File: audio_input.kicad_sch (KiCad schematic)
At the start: 4 parts

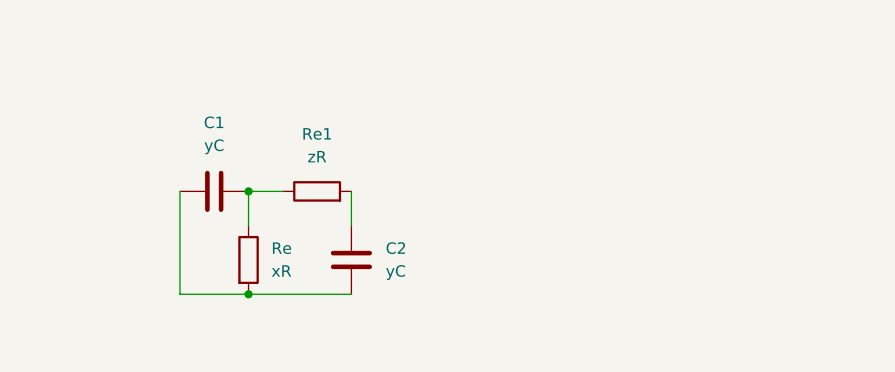
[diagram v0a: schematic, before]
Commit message: Rev 1
needs sensors, things like pull-up resistors and protection diodes, electrical rules check. also check SCL and SDA busses, variable resistors
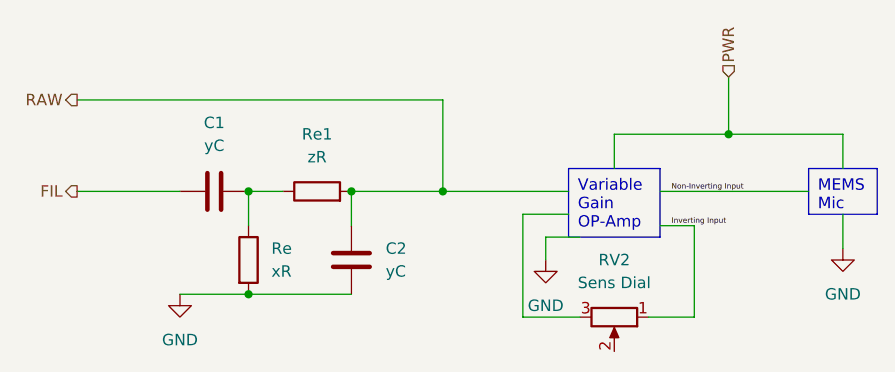
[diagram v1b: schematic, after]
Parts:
- added RV2: Sens Dial, Potentiometer_SMD:Potentiometer_ACP_CA6-VSMD_Vertical, symbol Device:R_Potentiometer
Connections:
- net GND: now reaches C2.1, Re.2
- net GND: no longer C1.1
- net RAW: now reaches C2.2, Re1.2
- new net FIL: C1.1
- new net Inverting Input: RV2.1
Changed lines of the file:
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@@
   (junction (at 148.59 92.71) (diameter 0) (color 0 0 0 0)
   )
+  (junction (at 201.93 86.36) (diameter 0) (color 0 0 0 0)
+  )
+  (junction (at 160.02 92.71) (diameter 0) (color 0 0 0 0)
+  )
+  (junction (at 170.18 92.71) (diameter 0) (color 0 0 0 0)
+  )
   (junction (at 148.59 104.14) (diameter 0) (color 0 0 0 0)
   )
+  (wire (pts (xy 181.61 97.79) (xy 181.61 100.33))
+    (stroke (width 0) (type default))
+  )
+  (wire (pts (xy 184.15 95.25) (xy 179.07 95.25))
+    (stroke (width 0) (type default))
+  )
+  (wire (pts (xy 185.42 97.79) (xy 181.61 97.79))
+    (stroke (width 0) (type default))
+  )
+  (wire (pts (xy 179.07 106.68) (xy 185.42 106.68))
+    (stroke (width 0) (type default))
+  )
+  (wire (pts (xy 198.12 106.68) (xy 198.12 96.52))
+    (stroke (width 0) (type default))
+  )
+  (wire (pts (xy 214.63 95.25) (xy 214.63 99.06))
+    (stroke (width 0) (type default))
+  )
+  (wire (pts (xy 194.31 92.71) (xy 210.82 92.71))
+    (stroke (width 0) (type default))
+  )
   (wire (pts (xy 140.97 104.14) (xy 148.59 104.14))
     (stroke (width 0) (type default))
@@
     (stroke (width 0) (type default))
   )
-  (wire (pts (xy 140.97 92.71) (xy 140.97 104.14))
+  (wire (pts (xy 179.07 95.25) (xy 179.07 106.68))
+    (stroke (width 0) (type default))
+  )
+  (wire (pts (xy 194.31 96.52) (xy 198.12 96.52))
     (stroke (width 0) (type default))
   )
@@
     (stroke (width 0) (type default))
   )
+  (wire (pts (xy 129.54 82.55) (xy 170.18 82.55))
+    (stroke (width 0) (type default))
+  )
+  (wire (pts (xy 201.93 80.01) (xy 201.93 86.36))
+    (stroke (width 0) (type default))
+  )
+  (wire (pts (xy 193.04 106.68) (xy 198.12 106.68))
+    (stroke (width 0) (type default))
+  )
+  (wire (pts (xy 160.02 92.71) (xy 170.18 92.71))
+    (stroke (width 0) (type default))
+  )
+  (wire (pts (xy 201.93 86.36) (xy 189.23 86.36))
+    (stroke (width 0) (type default))
+  )
   (wire (pts (xy 148.59 104.14) (xy 160.02 104.14))
     (stroke (width 0) (type default))
   )
+  (wire (pts (xy 184.15 92.71) (xy 170.18 92.71))
+    (stroke (width 0) (type default))
+  )
+  (wire (pts (xy 189.23 86.36) (xy 189.23 90.17))
+    (stroke (width 0) (type default))
+  )
+  (wire (pts (xy 170.18 82.55) (xy 170.18 92.71))
+    (stroke (width 0) (type default))
+  )
+  (wire (pts (xy 129.54 92.71) (xy 140.97 92.71))
+    (stroke (width 0) (type default))
+  )
   (wire (pts (xy 160.02 92.71) (xy 160.02 96.52))
     (stroke (width 0) (type default))
+  )
+  (wire (pts (xy 214.63 86.36) (xy 201.93 86.36))
+    (stroke (width 0) (type default))
+  )
+  (wire (pts (xy 214.63 90.17) (xy 214.63 86.36))
+    (stroke (width 0) (type default))
+  )
+  (text_box "Variable Gain OP-Amp"
+    (at 184.15 90.17 0) (size 10.16 7.62)
+    (stroke (width 0) (type default))
+    (fill (type none))
+    (effects (font (size 1.27 1.27)) (justify left top))
+  )
+  (text_box "MEMS Mic"
+    (at 210.82 90.17 0) (size 7.62 5.08)
+    (stroke (width 0) (type default))
+    (fill (type none))
+    (effects (font (size 1.27 1.27)) (justify left top))
+  )
+  (label "Non-Inverting Input" (at 195.58 92.71 0) (fields_autoplaced)
+    (effects (font (size 0.6 0.6)) (justify left bottom))
+  )
+  (label "Inverting Input" (at 195.58 96.52 0) (fields_autoplaced)
+    (effects (font (size 0.6 0.6)) (justify left bottom))
+  )
+  (hierarchical_label "FIL" (shape output) (at 129.54 92.71 180) (fields_autoplaced)
+    (effects (font (size 1.27 1.27)) (justify right))
+  )
+  (hierarchical_label "PWR" (shape input) (at 201.93 80.01 90) (fields_autoplaced)
+    (effects (font (size 1.27 1.27)) (justify left))
+  )
+  (hierarchical_label "RAW" (shape output) (at 129.54 82.55 180) (fields_autoplaced)
+    (effects (font (size 1.27 1.27)) (justify right))
   )
   (symbol (lib_id "Device:C") (at 160.02 100.33 180) (unit 1)
@@
         )
       )
+    )
+  )
+  (symbol (lib_id "power:GND") (at 181.61 100.33 0) (unit 1)
+    (in_bom yes) (on_board yes) (dnp no) (fields_autoplaced)
+    (property "Reference" "#PWR03" (at 181.61 106.68 0)
+      (effects (font (size 1.27 1.27)) hide)
+    )
+    (property "Value" "GND" (at 181.61 105.41 0)
+      (effects (font (size 1.27 1.27)))
+    )
+    (property "Footprint" "" (at 181.61 100.33 0)
+      (effects (font (size 1.27 1.27)) hide)
+    )
+    (property "Datasheet" "" (at 181.61 100.33 0)
+      (effects (font (size 1.27 1.27)) hide)
+    )
+    (pin "1")
+    (instances
+      (project "VibeLight"
+        (path "/704dec10-a4c2-4298-be85-193d9407f59f/964563b4-99e1-4b3d-857d-35f5fde5aa09"
+          (reference "#PWR03") (unit 1)
+        )
+      )
+    )
+  )
+  (symbol (lib_id "power:GND") (at 214.63 99.06 0) (unit 1)
+    (in_bom yes) (on_board yes) (dnp no) (fields_autoplaced)
+    (property "Reference" "#PWR02" (at 214.63 105.41 0)
+      (effects (font (size 1.27 1.27)) hide)
+    )
+    (property "Value" "GND" (at 214.63 104.14 0)
+      (effects (font (size 1.27 1.27)))
+    )
+    (property "Footprint" "" (at 214.63 99.06 0)
+      (effects (font (size 1.27 1.27)) hide)
+    )
+    (property "Datasheet" "" (at 214.63 99.06 0)
+      (effects (font (size 1.27 1.27)) hide)
+    )
+    (pin "1")
+    (instances
+      (project "VibeLight"
+        (path "/704dec10-a4c2-4298-be85-193d9407f59f/964563b4-99e1-4b3d-857d-35f5fde5aa09"
+          (reference "#PWR02") (unit 1)
+        )
+      )
+    )
+  )
+  (symbol (lib_id "Device:R_Potentiometer") (at 189.23 106.68 270) (unit 1)
+    (in_bom yes) (on_board yes) (dnp no) (fields_autoplaced)
+    (property "Reference" "RV2" (at 189.23 100.33 90)
+      (effects (font (size 1.27 1.27)))
+    )
+    (property "Value" "Sens Dial" (at 189.23 102.87 90)
+      (effects (font (size 1.27 1.27)))
+    )
+    (property "Footprint" "Potentiometer_SMD:Potentiometer_ACP_CA6-VSMD_Vertical" (at 189.23 106.68 0)
+      (effects (font (size 1.27 1.27)) hide)
+    )
+    (property "Datasheet" "~" (at 189.23 106.68 0)
+      (effects (font (size 1.27 1.27)) hide)
+    )
+    (pin "1")
+    (pin "2")
+    (pin "3")
+    (instances
+      (project "VibeLight"
+        (path "/704dec10-a4c2-4298-be85-193d9407f59f"
+          (reference "RV2") (unit 1)
+        )
+        (path "/704dec10-a4c2-4298-be85-193d9407f59f/964563b4-99e1-4b3d-857d-35f5fde5aa09"
+          (reference "RV1") (unit 1)
+        )
+      )
+    )
+  )
+  (symbol (lib_id "power:GND") (at 140.97 104.14 0) (unit 1)
+    (in_bom yes) (on_board yes) (dnp no) (fields_autoplaced)
+    (property "Reference" "#PWR01" (at 140.97 110.49 0)
+      (effects (font (size 1.27 1.27)) hide)
+    )
+    (property "Value" "GND" (at 140.97 109.22 0)
+      (effects (font (size 1.27 1.27)))
+    )
+    (property "Footprint" "" (at 140.97 104.14 0)
+      (effects (font (size 1.27 1.27)) hide)
+    )
+    (property "Datasheet" "" (at 140.97 104.14 0)
+      (effects (font (size 1.27 1.27)) hide)
+    )
+    (pin "1")
+    (instances
+      (project "VibeLight"
+        (path "/704dec10-a4c2-4298-be85-193d9407f59f/964563b4-99e1-4b3d-857d-35f5fde5aa09"
+          (reference "#PWR01") (unit 1)
+        )
+      )

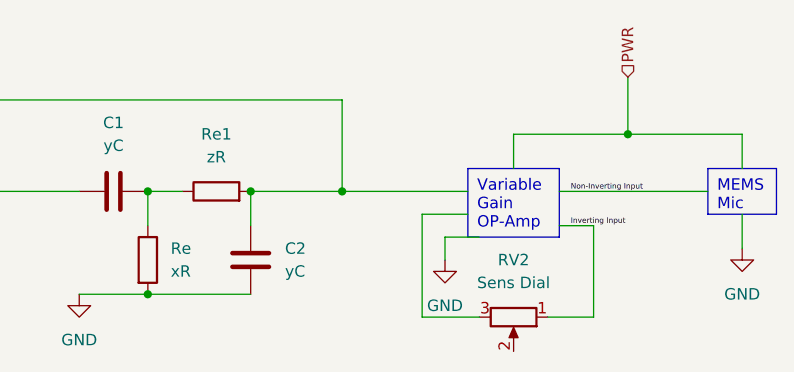
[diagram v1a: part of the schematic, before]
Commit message: added debug LED after Op-Amp
want battery status LED?
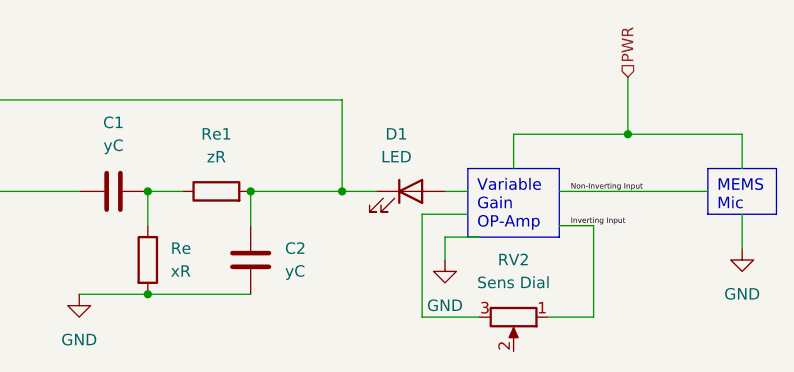
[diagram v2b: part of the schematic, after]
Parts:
- added D1: LED, symbol Device:LED
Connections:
- net RAW: now also D1.1 (K)
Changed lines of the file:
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@@
+    (stroke (width 0) (type default))
+  )
+  (wire (pts (xy 170.18 92.71) (xy 173.99 92.71))
     (stroke (width 0) (type default))
   )
@@
     (stroke (width 0) (type default))
   )
-  (wire (pts (xy 184.15 92.71) (xy 170.18 92.71))
+  (wire (pts (xy 181.61 92.71) (xy 184.15 92.71))
     (stroke (width 0) (type default))
   )
@@
         )
       )
+    )
+  )
+  (symbol (lib_id "Device:LED") (at 177.8 92.71 0) (unit 1)
+    (in_bom yes) (on_board yes) (dnp no) (fields_autoplaced)
+    (property "Reference" "D1" (at 176.2125 86.36 0)
+      (effects (font (size 1.27 1.27)))
+    )
+    (property "Value" "LED" (at 176.2125 88.9 0)
+      (effects (font (size 1.27 1.27)))
+    )
+    (property "Footprint" "" (at 177.8 92.71 0)
+      (effects (font (size 1.27 1.27)) hide)
+    )
+    (property "Datasheet" "~" (at 177.8 92.71 0)
+      (effects (font (size 1.27 1.27)) hide)
+    )
+    (pin "1")
+    (pin "2")
+    (instances
+      (project "VibeLight"
+        (path "/704dec10-a4c2-4298-be85-193d9407f59f/964563b4-99e1-4b3d-857d-35f5fde5aa09"
+          (reference "D1") (unit 1)
+        )
+      )

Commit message: misc changes during call
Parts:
- added Re: xR, Resistor_SMD:R_0603_1608Metric_Pad0.98x0.95mm_HandSolder, symbol Device:R
- D1: footprint (none) -> LED_SMD:LED_0603_1608Metric_Pad1.05x0.95mm_HandSolder
- RV2: value Sens Dial -> Intensity Dial; footprint Potentiometer_SMD:Potentiometer_ACP_CA6-VSMD_Vertical -> Potentiometer_SMD:Potentiometer_Bourns_TC33X_Vertical; Source (none) -> https://www.digikey.com/en/products/detail/bourns-inc/TC33X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
- Re, Re1: footprint Resistor_SMD:R_0805_2012Metric_Pad1.20x1.40mm_HandSolder -> Resistor_SMD:R_0603_1608Metric_Pad0.98x0.95mm_HandSolder
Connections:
- net GND: now also D1.1 (K)
- net Inverting Input: now also RV2.2; no longer RV2.1
- net RAW: now also Re.1; no longer D1.1 (K)
- net at D1.2 (A): now also Re.2
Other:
- moved on the sheet: D1
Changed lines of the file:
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@@
-    (stroke (width 0) (type default))
-  )
-  (wire (pts (xy 170.18 92.71) (xy 173.99 92.71))
     (stroke (width 0) (type default))
   )
@@
     (stroke (width 0) (type default))
   )
+  (wire (pts (xy 170.18 100.33) (xy 170.18 111.76))
+    (stroke (width 0) (type default))
+  )
   (wire (pts (xy 140.97 104.14) (xy 148.59 104.14))
     (stroke (width 0) (type default))
@@
     (stroke (width 0) (type default))
   )
+  (wire (pts (xy 189.23 110.49) (xy 193.04 110.49))
+    (stroke (width 0) (type default))
+  )
   (wire (pts (xy 148.59 92.71) (xy 148.59 96.52))
     (stroke (width 0) (type default))
   )
+  (wire (pts (xy 193.04 110.49) (xy 193.04 106.68))
+    (stroke (width 0) (type default))
+  )
   (wire (pts (xy 129.54 82.55) (xy 170.18 82.55))
     (stroke (width 0) (type default))
@@
     (stroke (width 0) (type default))
   )
-  (wire (pts (xy 181.61 92.71) (xy 184.15 92.71))
+  (wire (pts (xy 170.18 92.71) (xy 184.15 92.71))
     (stroke (width 0) (type default))
   )
@@
     (stroke (width 0) (type default))
   )
+  (wire (pts (xy 158.75 119.38) (xy 158.75 123.19))
+    (stroke (width 0) (type default))
+  )
   (wire (pts (xy 170.18 82.55) (xy 170.18 92.71))
     (stroke (width 0) (type default))
@@
   )
   (wire (pts (xy 214.63 86.36) (xy 201.93 86.36))
+    (stroke (width 0) (type default))
+  )
+  (wire (pts (xy 170.18 111.76) (xy 158.75 111.76))
     (stroke (width 0) (type default))
   )
@@
     )
   )
+  (symbol (lib_id "Device:R") (at 170.18 96.52 0) (unit 1)
+    (in_bom yes) (on_board yes) (dnp no) (fields_autoplaced)
+    (property "Reference" "Re" (at 172.72 95.25 0)
+      (effects (font (size 1.27 1.27)) (justify left))
+    )
+    (property "Value" "xR" (at 172.72 97.79 0)
+      (effects (font (size 1.27 1.27)) (justify left))
+    )
+    (property "Footprint" "Resistor_SMD:R_0603_1608Metric_Pad0.98x0.95mm_HandSolder" (at 168.402 96.52 90)
+      (effects (font (size 1.27 1.27)) hide)
+    )
+    (property "Datasheet" "~" (at 170.18 96.52 0)
+      (effects (font (size 1.27 1.27)) hide)
+    )
+    (pin "1")
+    (pin "2")
+    (instances
+      (project "VibeLight"
+        (path "/704dec10-a4c2-4298-be85-193d9407f59f"
+          (reference "Re") (unit 1)
+        )
+        (path "/704dec10-a4c2-4298-be85-193d9407f59f/964563b4-99e1-4b3d-857d-35f5fde5aa09"
+          (reference "Re3") (unit 1)
+        )
+      )
+    )
+  )
+  (symbol (lib_id "Device:R_Potentiometer") (at 185.42 110.49 0) (unit 1)
+    (in_bom yes) (on_board yes) (dnp no) (fields_autoplaced)
+    (property "Reference" "RV2" (at 182.88 109.22 0)
+      (effects (font (size 1.27 1.27)) (justify right))
+    )
+    (property "Value" "Intensity Dial" (at 182.88 111.76 0)
+      (effects (font (size 1.27 1.27)) (justify right))
+    )
+    (property "Footprint" "Potentiometer_SMD:Potentiometer_Bourns_TC33X_Vertical" (at 185.42 110.49 0)
+      (effects (font (size 1.27 1.27)) hide)
+    )
+    (property "Datasheet" "~" (at 185.42 110.49 0)
+      (effects (font (size 1.27 1.27)) hide)
+    )
+    (property "Source" "https://www.digikey.com/en/products/detail/bourns-inc/TC33X-2-103E/612858" (at 185.42 110.49 0)
+      (effects (font (size 1.27 1.27)) hide)
+    )
+    (pin "1")
+    (pin "2")
+    (pin "3")
+    (instances
+      (project "VibeLight"
+        (path "/704dec10-a4c2-4298-be85-193d9407f59f"
+          (reference "RV2") (unit 1)
+        )
+        (path "/704dec10-a4c2-4298-be85-193d9407f59f/964563b4-99e1-4b3d-857d-35f5fde5aa09"
+          (reference "RV3") (unit 1)
+        )
+      )
+    )
+  )
   (symbol (lib_id "power:GND") (at 181.61 100.33 0) (unit 1)
     (in_bom yes) (on_board yes) (dnp no) (fields_autoplaced)
@@
     )
   )
-  (symbol (lib_id "Device:LED") (at 177.8 92.71 0) (unit 1)
-    (in_bom yes) (on_board yes) (dnp no) (fields_autoplaced)
-    (property "Reference" "D1" (at 176.2125 86.36 0)
-      (effects (font (size 1.27 1.27)))
-    )
-    (property "Value" "LED" (at 176.2125 88.9 0)
-      (effects (font (size 1.27 1.27)))
-    )
-    (property "Footprint" "" (at 177.8 92.71 0)
-      (effects (font (size 1.27 1.27)) hide)
-    )
-    (property "Datasheet" "~" (at 177.8 92.71 0)
+  (symbol (lib_id "Device:LED") (at 158.75 115.57 90) (unit 1)
+    (in_bom yes) (on_board yes) (dnp no) (fields_autoplaced)
+    (property "Reference" "D1" (at 162.56 115.8875 90)
+      (effects (font (size 1.27 1.27)) (justify right))
+    )
+    (property "Value" "LED" (at 162.56 118.4275 90)
+      (effects (font (size 1.27 1.27)) (justify right))
+    )
+    (property "Footprint" "LED_SMD:LED_0603_1608Metric_Pad1.05x0.95mm_HandSolder" (at 158.75 115.57 0)
+      (effects (font (size 1.27 1.27)) hide)
+    )
+    (property "Datasheet" "~" (at 158.75 115.57 0)
       (effects (font (size 1.27 1.27)) hide)
     )
@@
     )
   )
+  (symbol (lib_id "power:GND") (at 158.75 123.19 0) (unit 1)
+    (in_bom yes) (on_board yes) (dnp no) (fields_autoplaced)
+    (property "Reference" "#PWR020" (at 158.75 129.54 0)
+      (effects (font (size 1.27 1.27)) hide)
+    )
+    (property "Value" "GND" (at 158.75 128.27 0)
+      (effects (font (size 1.27 1.27)))
+    )
+    (property "Footprint" "" (at 158.75 123.19 0)
+      (effects (font (size 1.27 1.27)) hide)
+    )
+    (property "Datasheet" "" (at 158.75 123.19 0)
+      (effects (font (size 1.27 1.27)) hide)
+    )
+    (pin "1")
+    (instances
+      (project "VibeLight"
+        (path "/704dec10-a4c2-4298-be85-193d9407f59f/964563b4-99e1-4b3d-857d-35f5fde5aa09"
+          (reference "#PWR020") (unit 1)
+        )
+      )
+    )
+  )
   (symbol (lib_id "power:GND") (at 214.63 99.06 0) (unit 1)
     (in_bom yes) (on_board yes) (dnp no) (fields_autoplaced)
@@
     )
   )
-  (symbol (lib_id "Device:R_Potentiometer") (at 189.23 106.68 270) (unit 1)
-    (in_bom yes) (on_board yes) (dnp no) (fields_autoplaced)
-    (property "Reference" "RV2" (at 189.23 100.33 90)
-      (effects (font (size 1.27 1.27)))
-    )
-    (property "Value" "Sens Dial" (at 189.23 102.87 90)
-      (effects (font (size 1.27 1.27)))
-    )
-    (property "Footprint" "Potentiometer_SMD:Potentiometer_ACP_CA6-VSMD_Vertical" (at 189.23 106.68 0)
-      (effects (font (size 1.27 1.27)) hide)
-    )
-    (property "Datasheet" "~" (at 189.23 106.68 0)
-      (effects (font (size 1.27 1.27)) hide)
-    )
-    (pin "1")
-    (pin "2")
-    (pin "3")
-    (instances
-      (project "VibeLight"
-        (path "/704dec10-a4c2-4298-be85-193d9407f59f"
-          (reference "RV2") (unit 1)
-        )
-        (path "/704dec10-a4c2-4298-be85-193d9407f59f/964563b4-99e1-4b3d-857d-35f5fde5aa09"
-          (reference "RV1") (unit 1)
-        )
-      )
-    )
-  )
   (symbol (lib_id "power:GND") (at 140.97 104.14 0) (unit 1)
     (in_bom yes) (on_board yes) (dnp no) (fields_autoplaced)
@@
       (effects (font (size 1.27 1.27)))
     )
-    (property "Footprint" "Resistor_SMD:R_0805_2012Metric_Pad1.20x1.40mm_HandSolder" (at 156.21 94.488 90)
+    (property "Footprint" "Resistor_SMD:R_0603_1608Metric_Pad0.98x0.95mm_HandSolder" (at 156.21 94.488 90)
       (effects (font (size 1.27 1.27)) hide)
     )
@@
       (effects (font (size 1.27 1.27)) (justify left))
     )
-    (property "Footprint" "Resistor_SMD:R_0805_2012Metric_Pad1.20x1.40mm_HandSolder" (at 146.812 100.33 90)
-      (effects (font (size 1.27 1.27)) hide)
-    )
+    (property "Footprint" "Resistor_SMD:R_0603_1608Metric_Pad0.98x0.95mm_HandSolder" (at 146.812 100.33 90)
+      (effects (font (size 1.27 1.27)) hide)
+    )

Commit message: started work on pcb layout
started work on pcb layout
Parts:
- added C5, C6, C7: C, Capacitor_SMD:C_0603_1608Metric_Pad1.08x0.95mm_HandSolder, symbol Device:C
- added R6: R, Resistor_SMD:R_0603_1608Metric_Pad0.98x0.95mm_HandSolder, symbol Device:R
- added U1: AD8603, Package_TO_SOT_SMD:TSOT-23-5, symbol Amplifier_Operational:AD8603
- RV2: value Intensity Dial -> Sens Dial
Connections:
- net GND: now also RV2.3, C5.1, R6.2, U1.2 (V-)
- net PWR: now also C5.2, U1.5 (V+)
- net RAW: now also RV2.1, U1.1
- net Inverting Input: no longer names the net of RV2.2
- net Inverting Input: now also C7.1, U1.4 (-)
- new net: C7.2, R6.1
- new net: C6.1, U1.3 (+)
- new net MEMS Mic/2_OUT: C6.2
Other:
- added sheet MEMS Mic (untitled.kicad_sch)

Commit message: Changes from DR call
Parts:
- removed C6: C, Capacitor_SMD:C_0603_1608Metric_Pad1.08x0.95mm_HandSolder, symbol Device:C
- removed R6: R, Resistor_SMD:R_0603_1608Metric_Pad0.98x0.95mm_HandSolder, symbol Device:R
- added C9: 1uF, Capacitor_SMD:C_0603_1608Metric_Pad1.08x0.95mm_HandSolder, symbol Device:C
- added Re (x3): 10K, Resistor_SMD:R_0603_1608Metric_Pad0.98x0.95mm_HandSolder, symbol Device:R
- C7: value C -> 4.7uF
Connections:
- net GND: now also C9.1, Re.2; no longer RV2.3
- net MEMS Mic/2_OUT: now also C7.2
- net at RV2.2, U1.4 (-): now also Re.1; no longer C7.1
- net at U1.3 (+): now also C9.2, Re.1, Re.2
- net PWR renamed +3V3
- net +3V3: now also Re.1
- new net: C7.1, Re.2
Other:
- note added: "Ref circuit https://cdn.sparkfun.com/assets/c/3/7/5/e/SparkFun_Analog_MEMS_Microphone_Breakout_ICS40180_Schematic.pdf?_gl=1*4lbdek*_ga*MTg1NTQyNzYzOC4xNjkxMDc0MDIx*_ga_T369JS7J9N*MTY5MTA3NDAyMS4xLjAuMTY5MTA3NDAyMS42MC4wLjA."
- moved on the sheet: C7

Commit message: pcB rev2
need to fix reference texts on PCB, figure out MEMs mic wiring
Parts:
- C1: value yC -> C
- C2: value yC -> 1 uF
- C5: value C -> 100 nF
- Re: value xR -> R
- Re1: value zR -> 620R
- renumbered U1 to OpAmp1
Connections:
- net +3V3: no longer C5.2
- net FIL: now also C2.2, Re.1, Re1.2; no longer C1.1
- net GND: now also RV2.3
- net RAW: now also Re1.1; no longer C2.2, Re.1, Re1.2
- net at C9.2, OpAmp1.3 (+), Re.1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: now also Re.1
- net at OpAmp1.4 (-), RV2.2: now also C1.1; no longer Re.1
- net at C1.2, Re.1: no longer Re1.1
- new net PWR: C5.2
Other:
- moved on the sheet: C2, C5, C7, C9, D1, OpAmp1, RV2, Re, Re1
